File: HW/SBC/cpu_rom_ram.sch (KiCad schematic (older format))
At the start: 6 parts, among them U1 WD65C02_, U2 28C256, U3 AS6C62256A

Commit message: Added path to 65xx library
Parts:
- U2: symbol 28C256 -> 28C256-RESCUE-pluto
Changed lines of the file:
@@
 EESchema Schematic File Version 2
+LIBS:pluto-rescue
 LIBS:power
 LIBS:device
@@
 ~ROMSEL
 $Comp
-L 28C256 U2
+L 28C256-RESCUE-pluto U2
 U 1 1 59386D85
 P 5775 2300
+AR Path="/59386D85" Ref="U2"  Part="1"
+AR Path="/58D5892B/59386D85" Ref="U2"  Part="1"
 F 0 "U2" H 5975 3300 50  0000 C CNN
 F 1 "28C256" H 6075 1300 50  0000 C CNN

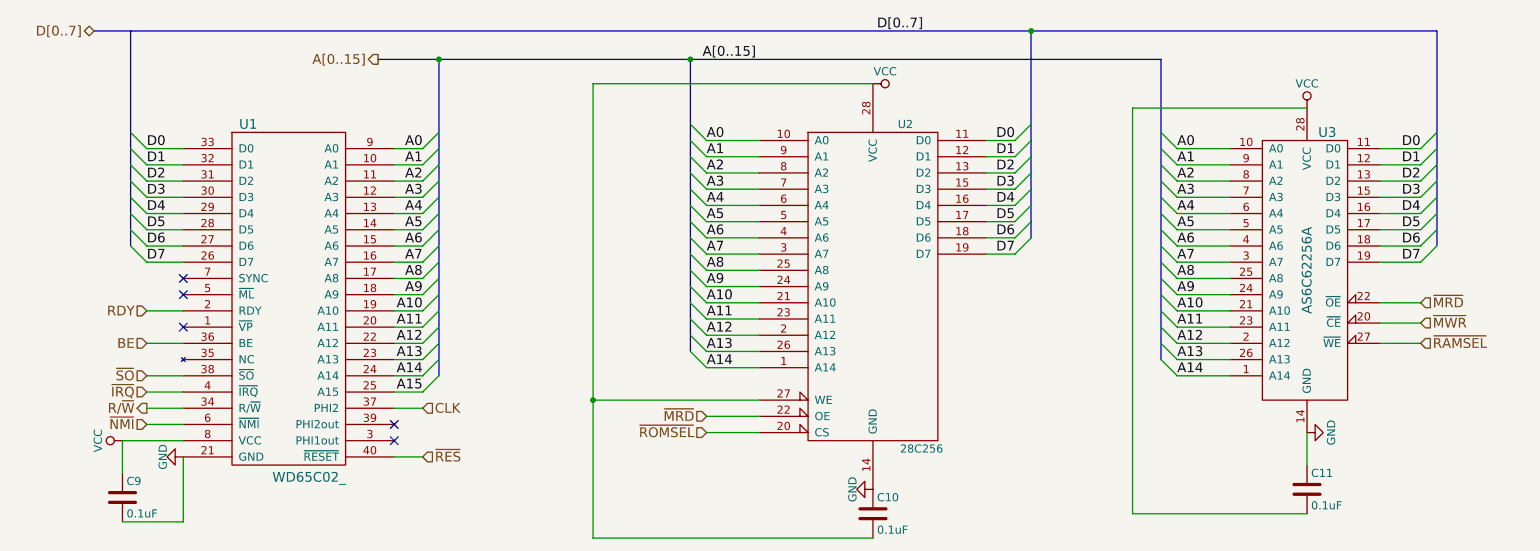
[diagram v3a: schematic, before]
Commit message: Update of test program to test both VIA.
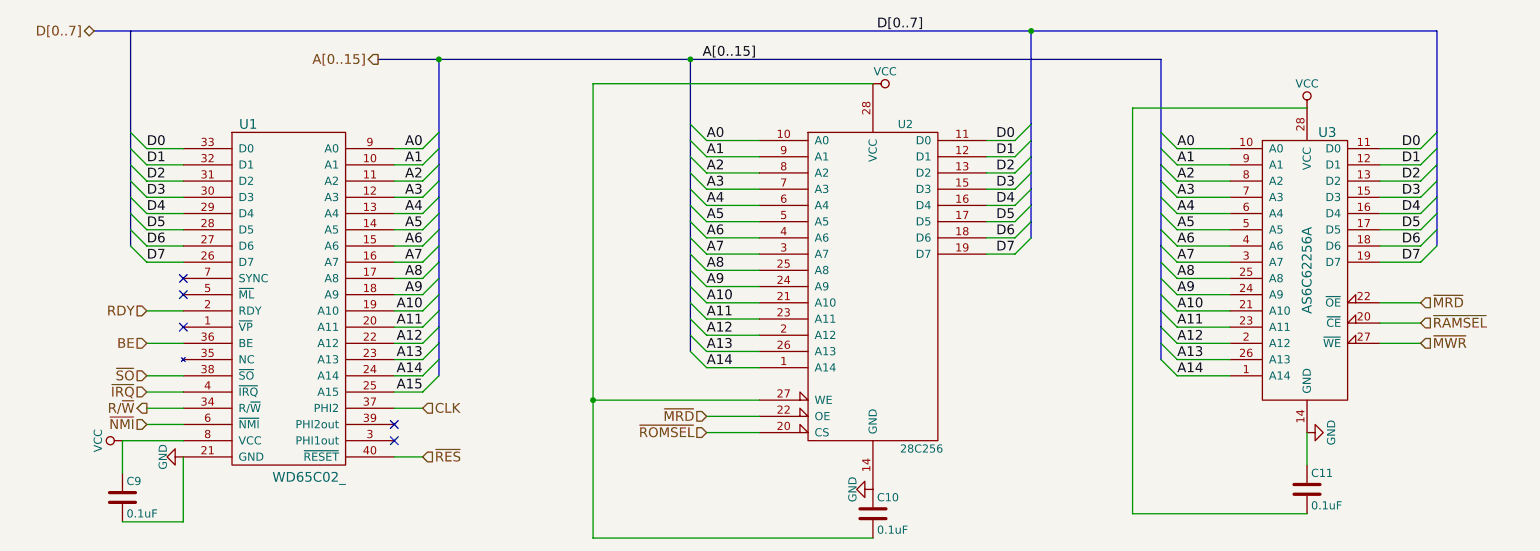
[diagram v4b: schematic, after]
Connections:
- net ~MWR: now also U3.27 (~WE); no longer U3.20 (~CE)
- net ~RAMSEL: now also U3.20 (~CE); no longer U3.27 (~WE)
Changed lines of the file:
@@
 	4050 3850 5775 3850
 Wire Wire Line
-	4050 1050 4050 3850
+	4050 1050 4050 3000
+Wire Wire Line
+	4050 3000 4050 3850
 Wire Wire Line
 	4050 1050 5775 1050
@@
 Connection ~ 4050 3000
 Wire Bus Line
-	3100 900  3100 2850
+	3100 900  3100 1350
 Wire Bus Line
-	4650 900  4650 2700
+	3100 1350 3100 1450
 Wire Bus Line
-	7550 900  7550 2750
+	3100 1450 3100 1550
 Wire Bus Line
-	1200 725  1200 2050
+	3100 1550 3100 1650
 Wire Bus Line
-	6750 725  6750 2000
+	3100 1650 3100 1750
 Wire Bus Line
-	9250 725  9250 2050
+	3100 1750 3100 1850
 Wire Bus Line
-	975  725  9250 725
+	3100 1850 3100 1950
+Wire Bus Line
+	3100 1950 3100 2050
+Wire Bus Line
+	3100 2050 3100 2150
+Wire Bus Line
+	3100 2150 3100 2250
+Wire Bus Line
+	3100 2250 3100 2350
+Wire Bus Line
+	3100 2350 3100 2450
+Wire Bus Line
+	3100 2450 3100 2550
+Wire Bus Line
+	3100 2550 3100 2650
+Wire Bus Line
+	3100 2650 3100 2750
+Wire Bus Line
+	3100 2750 3100 2850
+Wire Bus Line
+	4650 900  4650 1300
+Wire Bus Line
+	4650 1300 4650 1400
+Wire Bus Line
+	4650 1400 4650 1500
+Wire Bus Line
+	4650 1500 4650 1600
+Wire Bus Line
+	4650 1600 4650 1700
+Wire Bus Line
+	4650 1700 4650 1800
+Wire Bus Line
+	4650 1800 4650 1900
+Wire Bus Line
+	4650 1900 4650 2000
+Wire Bus Line
+	4650 2000 4650 2100
+Wire Bus Line
+	4650 2100 4650 2200
+Wire Bus Line
+	4650 2200 4650 2300
+Wire Bus Line
+	4650 2300 4650 2400
+Wire Bus Line
+	4650 2400 4650 2500
+Wire Bus Line
+	4650 2500 4650 2600
+Wire Bus Line
+	4650 2600 4650 2700
+Wire Bus Line
+	7550 900  7550 1350
+Wire Bus Line
+	7550 1350 7550 1450
+Wire Bus Line
+	7550 1450 7550 1550
+Wire Bus Line
+	7550 1550 7550 1650
+Wire Bus Line
+	7550 1650 7550 1750
+Wire Bus Line
+	7550 1750 7550 1850
+Wire Bus Line
+	7550 1850 7550 1950
+Wire Bus Line
+	7550 1950 7550 2050
+Wire Bus Line
+	7550 2050 7550 2150
+Wire Bus Line
+	7550 2150 7550 2250
+Wire Bus Line
+	7550 2250 7550 2350
+Wire Bus Line
+	7550 2350 7550 2450
+Wire Bus Line
+	7550 2450 7550 2550
+Wire Bus Line
+	7550 2550 7550 2650
+Wire Bus Line
+	7550 2650 7550 2750
+Wire Bus Line
+	1200 725  1200 1350
+Wire Bus Line
+	1200 1350 1200 1450
+Wire Bus Line
+	1200 1450 1200 1550
+Wire Bus Line
+	1200 1550 1200 1650
+Wire Bus Line
+	1200 1650 1200 1750
+Wire Bus Line
+	1200 1750 1200 1850
+Wire Bus Line
+	1200 1850 1200 1950
+Wire Bus Line
+	1200 1950 1200 2050
+Wire Bus Line
+	6750 725  6750 1300
+Wire Bus Line
+	6750 1300 6750 1400
+Wire Bus Line
+	6750 1400 6750 1500
+Wire Bus Line
+	6750 1500 6750 1600
+Wire Bus Line
+	6750 1600 6750 1700
+Wire Bus Line
+	6750 1700 6750 1800
+Wire Bus Line
+	6750 1800 6750 1900
+Wire Bus Line
+	6750 1900 6750 2000
+Wire Bus Line
+	9250 725  9250 1350
+Wire Bus Line
+	9250 1350 9250 1450
+Wire Bus Line
+	9250 1450 9250 1550
+Wire Bus Line
+	9250 1550 9250 1650
+Wire Bus Line
+	9250 1650 9250 1750
+Wire Bus Line
+	9250 1750 9250 1850
+Wire Bus Line
+	9250 1850 9250 1950
+Wire Bus Line
+	9250 1950 9250 2050
+Wire Bus Line
+	975  725  6750 725
+Wire Bus Line
+	6750 725  9250 725
 Text HLabel 975  725  0    60   BiDi ~ 0
 D[0..7]
 Wire Bus Line
-	2725 900  7550 900
+	2725 900  3100 900
+Wire Bus Line
+	3100 900  4650 900
+Wire Bus Line
+	4650 900  7550 900
 Connection ~ 6750 725
 Connection ~ 4650 900
@@
 Text HLabel 9150 2400 2    60   Input ~ 0
 ~MRD
+Text HLabel 9150 2650 2    60   Input ~ 0
+~MWR
 Text HLabel 9150 2525 2    60   Input ~ 0
-~MWR
-Text HLabel 9150 2650 2    60   Input ~ 0
 ~RAMSEL
 Text HLabel 4750 3100 0    60   Input ~ 0

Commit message: Small changes to comments.
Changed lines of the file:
@@
 	4050 3850 5775 3850
 Wire Wire Line
-	4050 1050 4050 3000
-Wire Wire Line
-	4050 3000 4050 3850
+	4050 1050 4050 3850
 Wire Wire Line
 	4050 1050 5775 1050
@@
 Connection ~ 4050 3000
 Wire Bus Line
-	3100 900  3100 1350
+	3100 900  3100 2850
 Wire Bus Line
-	3100 1350 3100 1450
+	4650 900  4650 2700
 Wire Bus Line
-	3100 1450 3100 1550
+	7550 900  7550 2750
 Wire Bus Line
-	3100 1550 3100 1650
+	1200 725  1200 2050
 Wire Bus Line
-	3100 1650 3100 1750
+	6750 725  6750 2000
 Wire Bus Line
-	3100 1750 3100 1850
+	9250 725  9250 2050
 Wire Bus Line
-	3100 1850 3100 1950
-Wire Bus Line
-	3100 1950 3100 2050
-Wire Bus Line
-	3100 2050 3100 2150
-Wire Bus Line
-	3100 2150 3100 2250
-Wire Bus Line
-	3100 2250 3100 2350
-Wire Bus Line
-	3100 2350 3100 2450
-Wire Bus Line
-	3100 2450 3100 2550
-Wire Bus Line
-	3100 2550 3100 2650
-Wire Bus Line
-	3100 2650 3100 2750
-Wire Bus Line
-	3100 2750 3100 2850
-Wire Bus Line
-	4650 900  4650 1300
-Wire Bus Line
-	4650 1300 4650 1400
-Wire Bus Line
-	4650 1400 4650 1500
-Wire Bus Line
-	4650 1500 4650 1600
-Wire Bus Line
-	4650 1600 4650 1700
-Wire Bus Line
-	4650 1700 4650 1800
-Wire Bus Line
-	4650 1800 4650 1900
-Wire Bus Line
-	4650 1900 4650 2000
-Wire Bus Line
-	4650 2000 4650 2100
-Wire Bus Line
-	4650 2100 4650 2200
-Wire Bus Line
-	4650 2200 4650 2300
-Wire Bus Line
-	4650 2300 4650 2400
-Wire Bus Line
-	4650 2400 4650 2500
-Wire Bus Line
-	4650 2500 4650 2600
-Wire Bus Line
-	4650 2600 4650 2700
-Wire Bus Line
-	7550 900  7550 1350
-Wire Bus Line
-	7550 1350 7550 1450
-Wire Bus Line
-	7550 1450 7550 1550
-Wire Bus Line
-	7550 1550 7550 1650
-Wire Bus Line
-	7550 1650 7550 1750
-Wire Bus Line
-	7550 1750 7550 1850
-Wire Bus Line
-	7550 1850 7550 1950
-Wire Bus Line
-	7550 1950 7550 2050
-Wire Bus Line
-	7550 2050 7550 2150
-Wire Bus Line
-	7550 2150 7550 2250
-Wire Bus Line
-	7550 2250 7550 2350
-Wire Bus Line
-	7550 2350 7550 2450
-Wire Bus Line
-	7550 2450 7550 2550
-Wire Bus Line
-	7550 2550 7550 2650
-Wire Bus Line
-	7550 2650 7550 2750
-Wire Bus Line
-	1200 725  1200 1350
-Wire Bus Line
-	1200 1350 1200 1450
-Wire Bus Line
-	1200 1450 1200 1550
-Wire Bus Line
-	1200 1550 1200 1650
-Wire Bus Line
-	1200 1650 1200 1750
-Wire Bus Line
-	1200 1750 1200 1850
-Wire Bus Line
-	1200 1850 1200 1950
-Wire Bus Line
-	1200 1950 1200 2050
-Wire Bus Line
-	6750 725  6750 1300
-Wire Bus Line
-	6750 1300 6750 1400
-Wire Bus Line
-	6750 1400 6750 1500
-Wire Bus Line
-	6750 1500 6750 1600
-Wire Bus Line
-	6750 1600 6750 1700
-Wire Bus Line
-	6750 1700 6750 1800
-Wire Bus Line
-	6750 1800 6750 1900
-Wire Bus Line
-	6750 1900 6750 2000
-Wire Bus Line
-	9250 725  9250 1350
-Wire Bus Line
-	9250 1350 9250 1450
-Wire Bus Line
-	9250 1450 9250 1550
-Wire Bus Line
-	9250 1550 9250 1650
-Wire Bus Line
-	9250 1650 9250 1750
-Wire Bus Line
-	9250 1750 9250 1850
-Wire Bus Line
-	9250 1850 9250 1950
-Wire Bus Line
-	9250 1950 9250 2050
-Wire Bus Line
-	975  725  6750 725
-Wire Bus Line
-	6750 725  9250 725
+	975  725  9250 725
 Text HLabel 975  725  0    60   BiDi ~ 0
 D[0..7]
 Wire Bus Line
-	2725 900  3100 900
-Wire Bus Line
-	3100 900  4650 900
-Wire Bus Line
-	4650 900  7550 900
+	2725 900  7550 900
 Connection ~ 6750 725
 Connection ~ 4650 900
